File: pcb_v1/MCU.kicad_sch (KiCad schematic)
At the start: 12 parts, among them U4 ESP32-S3-MINI-1, U6 STM32F103RETx

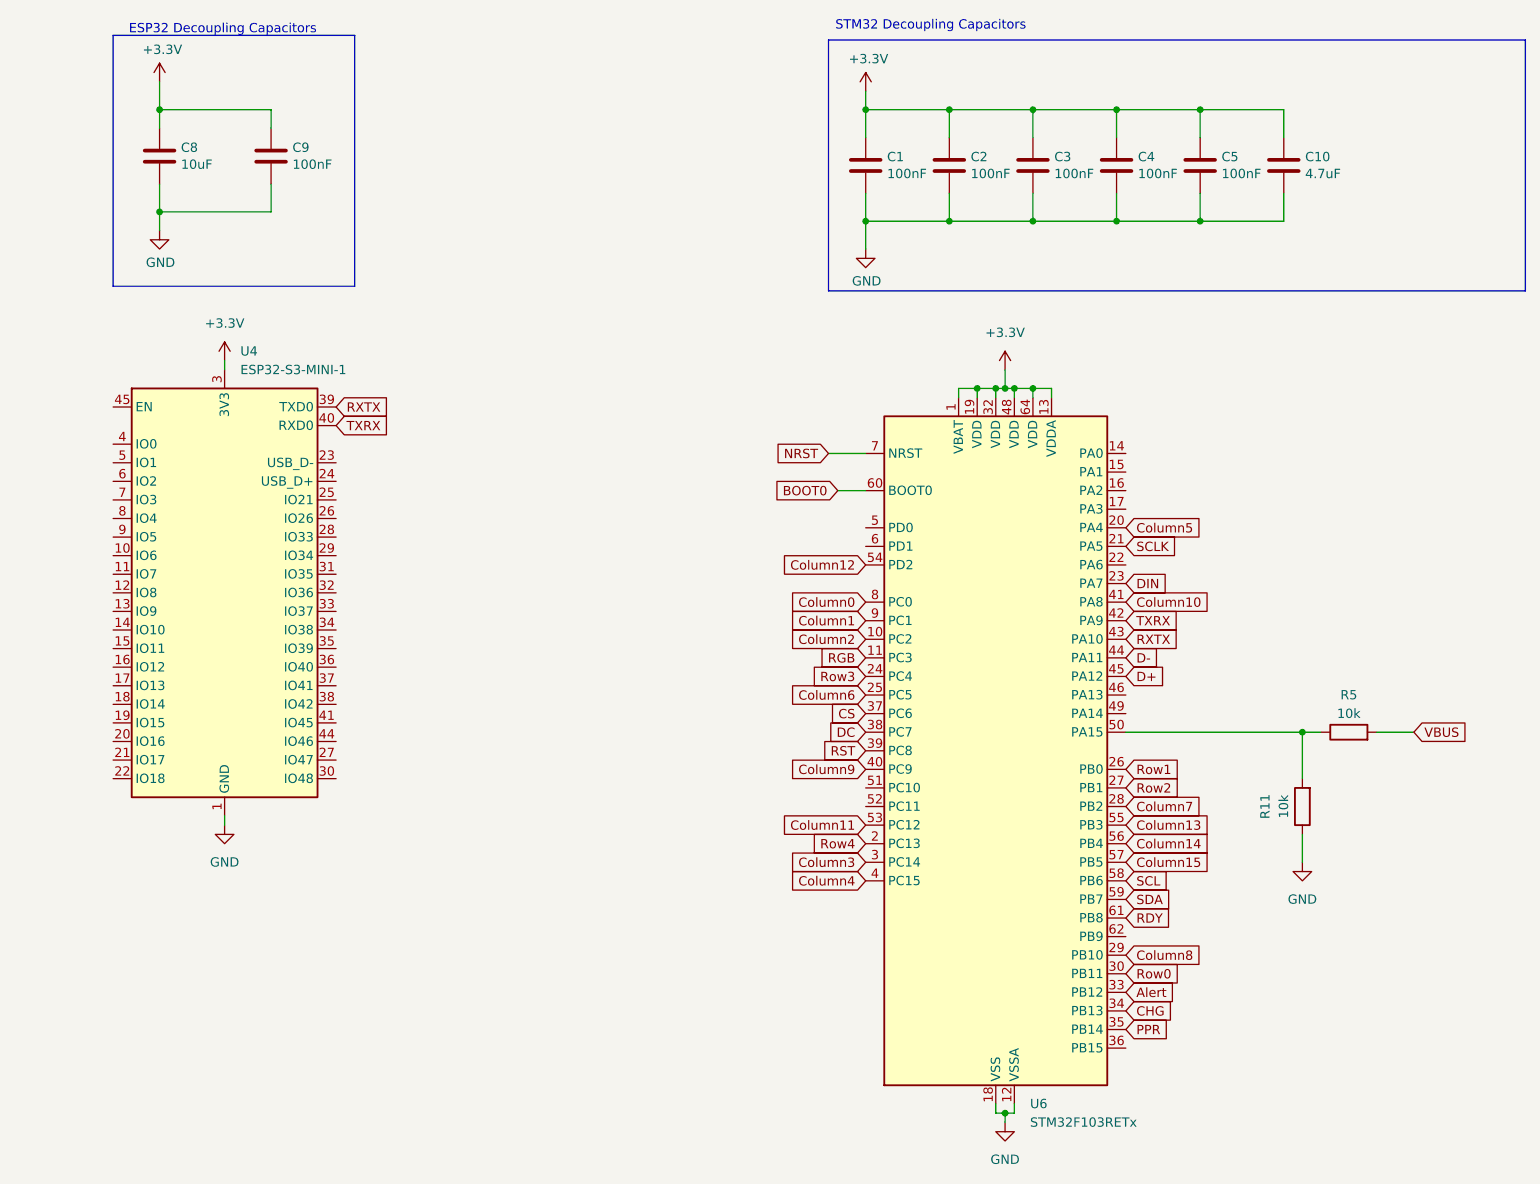
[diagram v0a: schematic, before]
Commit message: Finished 4 layer design
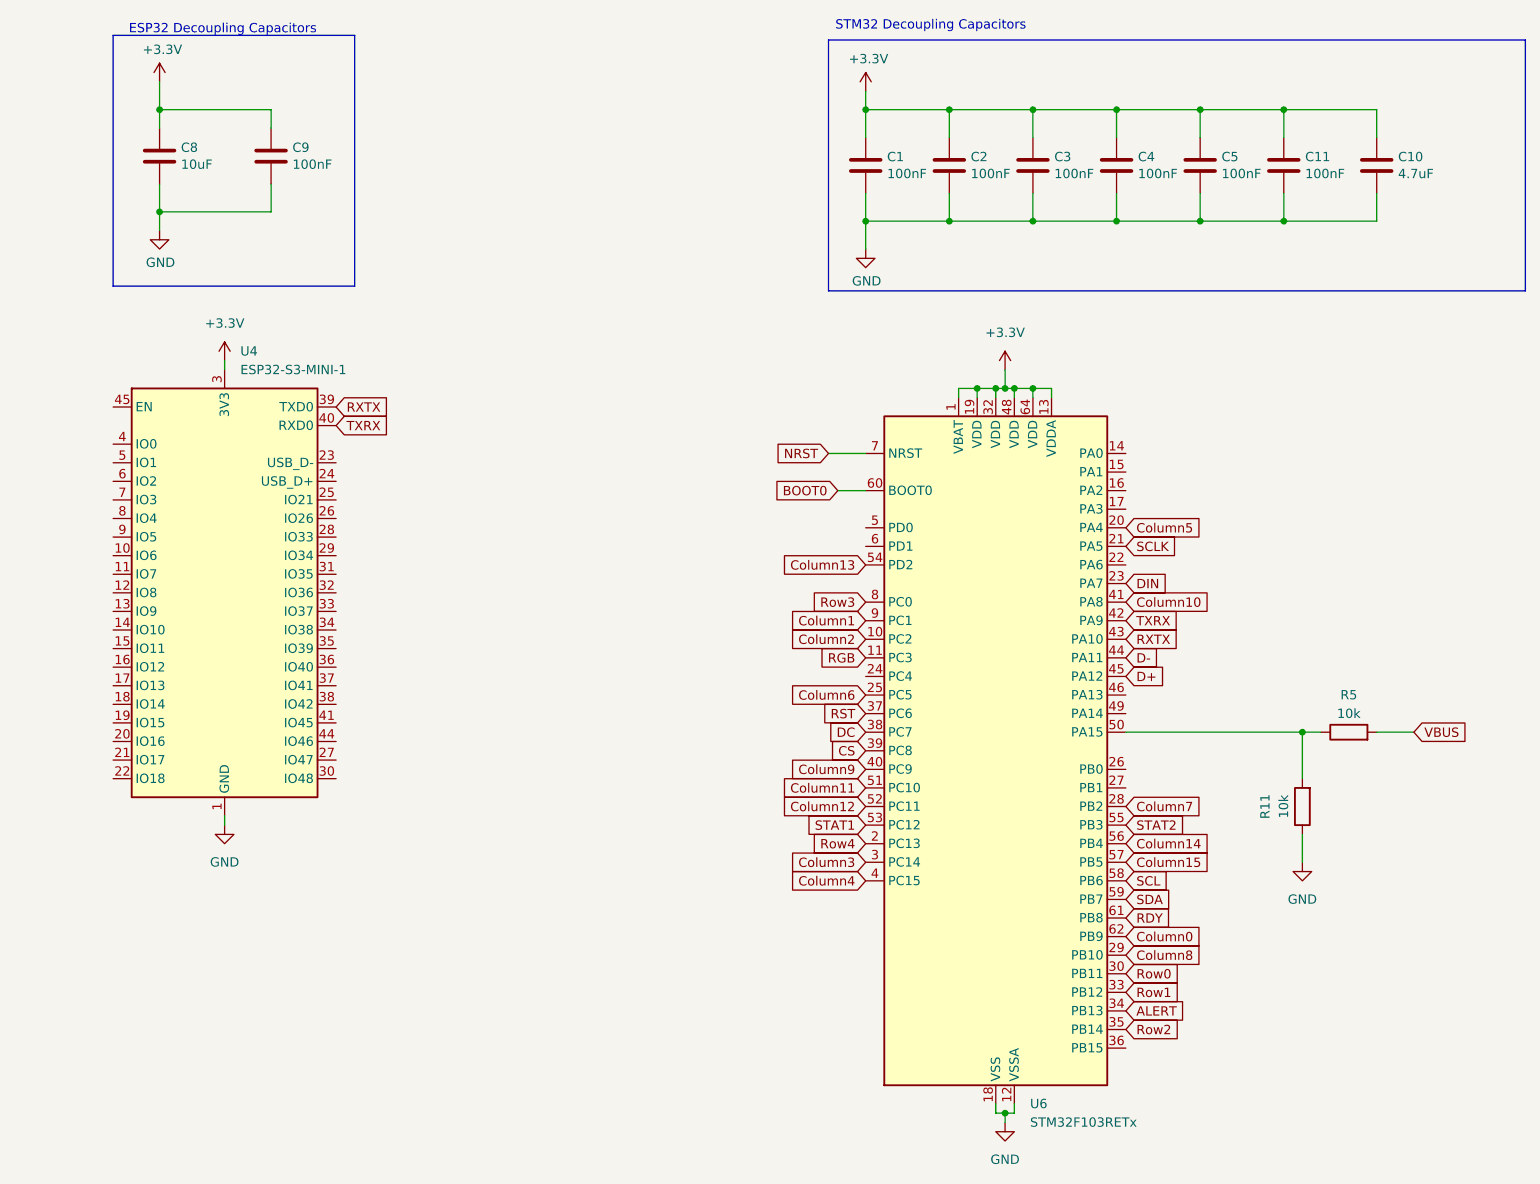
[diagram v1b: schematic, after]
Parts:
- added C11: 100nF, GRM1555C2A101GA01D:CAPC1005X55N, symbol Device:C
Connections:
- net Alert is gone; now on net Row1: U6.33 (PB12)
- net PPR is gone; now on net Row2: U6.35 (PB14)
- net +3.3V: now also C11.1
- net CS: now also U6.39 (PC8); no longer U6.37 (PC6)
- net Column0: now also U6.62 (PB9); no longer U6.8 (PC0)
- net Column11: now also U6.51 (PC10); no longer U6.53 (PC12)
- net Column12: now also U6.52 (PC11); no longer U6.54 (PD2)
- net Column13: now also U6.54 (PD2); no longer U6.55 (PB3)
- net GND: now also C11.2
- net RST: now also U6.37 (PC6); no longer U6.39 (PC8)
- net Row1: no longer U6.26 (PB0)
- net Row2: no longer U6.27 (PB1)
- net Row3: now also U6.8 (PC0); no longer U6.24 (PC4)
- net CHG renamed ALERT
- new net STAT1: U6.53 (PC12)
- new net STAT2: U6.55 (PB3)
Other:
- moved on the sheet: C10

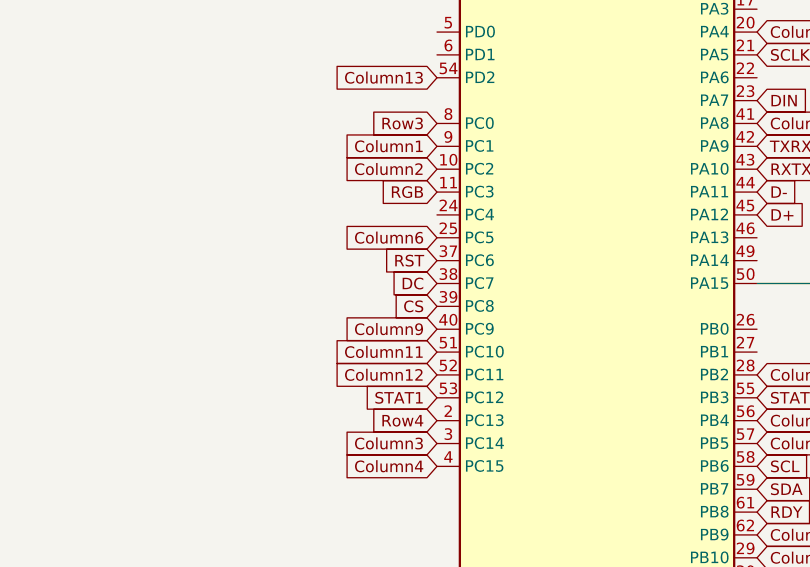
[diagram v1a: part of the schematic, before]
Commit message: Reverse polarity on pins
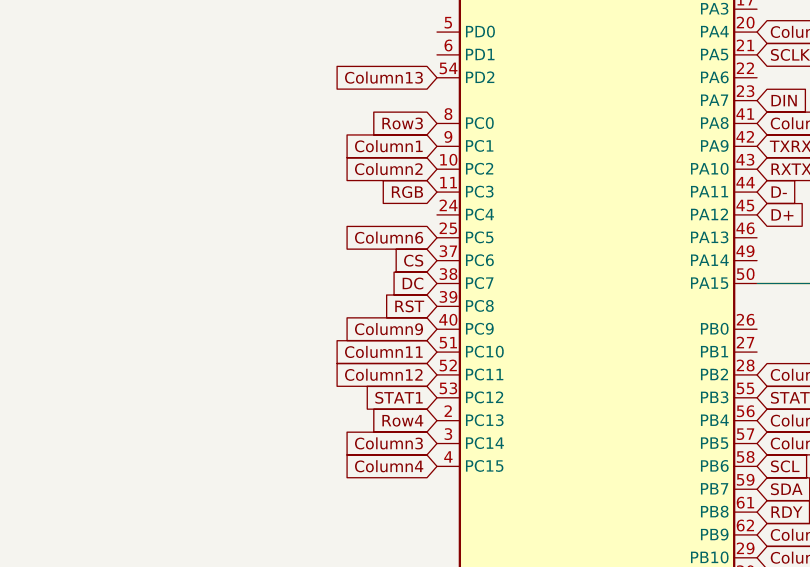
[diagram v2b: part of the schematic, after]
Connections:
- net CS: now also U6.37 (PC6); no longer U6.39 (PC8)
- net RST: now also U6.39 (PC8); no longer U6.37 (PC6)
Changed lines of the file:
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@@
+		)
+	)
+	(global_label "RST"
+		(shape input)
+		(at 127 118.11 180)
+		(fields_autoplaced yes)
+		(effects
+			(font
+				(size 1.27 1.27)
+			)
+			(justify right)
+		)
+		(property "Intersheetrefs" "${INTERSHEET_REFS}"
+			(at 120.5677 118.11 0)
+			(effects
+				(font
+					(size 1.27 1.27)
+				)
+				(justify right)
+				(hide yes)
+			)
 		)
 	)
@@
 		)
 	)
+	(global_label "CS"
+		(shape input)
+		(at 127 113.03 180)
+		(fields_autoplaced yes)
+		(effects
+			(font
+				(size 1.27 1.27)
+			)
+			(justify right)
+		)
+		(property "Intersheetrefs" "${INTERSHEET_REFS}"
+			(at 121.5353 113.03 0)
+			(effects
+				(font
+					(size 1.27 1.27)
+				)
+				(justify right)
+				(hide yes)
+			)
+		)
+	)
 	(global_label "RXTX"
 		(shape input)
@@
 		)
 	)
-	(global_label "CS"
-		(shape input)
-		(at 127 118.11 180)
-		(fields_autoplaced yes)
-		(effects
-			(font
-				(size 1.27 1.27)
-			)
-			(justify right)
-		)
-		(property "Intersheetrefs" "${INTERSHEET_REFS}"
-			(at 121.5353 118.11 0)
-			(effects
-				(font
-					(size 1.27 1.27)
-				)
-				(justify right)
-				(hide yes)
-			)
-		)
-	)
 	(global_label "Column12"
 		(shape input)
@@
 				(hide yes)
 			)
-		)
-	)
-	(global_label "RST"
-		(shape input)
-		(at 127 113.03 180)
-		(fields_autoplaced yes)
-		(effects
-			(font
-				(size 1.27 1.27)
-			)
-			(justify right)
-		)
-		(property "Intersheetrefs" "${INTERSHEET_REFS}"
-			(at 120.5677 113.03 0)
-			(effects
-				(font
-					(size 1.27 1.27)
-				)
-				(justify right)
-				(hide yes)
-			)

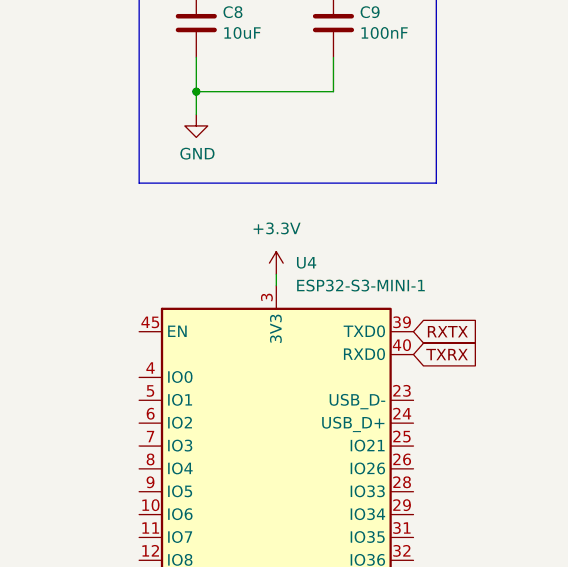
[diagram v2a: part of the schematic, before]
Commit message: Included resistors for EN/GPIO0 on ESP32
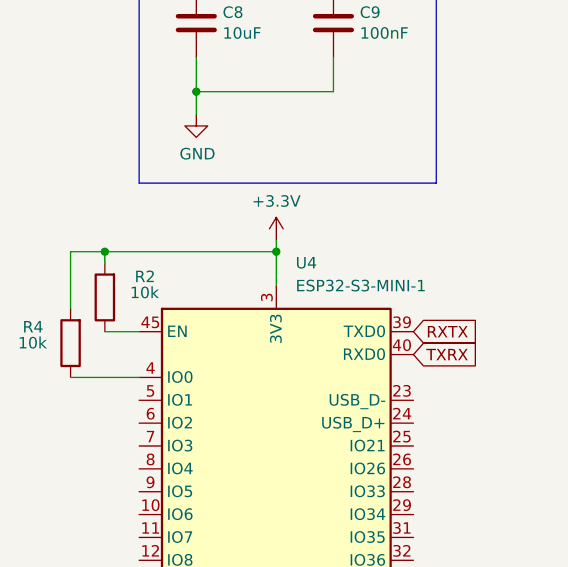
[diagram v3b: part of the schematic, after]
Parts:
- added R2, R4: 10k, RC0402FR-7D4K7L:RESC1005X40N, symbol ScottoKeebs:Placeholder_Resistor
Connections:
- net +3.3V: now also R2.2, R4.2
- net at U4.4 (IO0): now also R4.1
- net at U4.45 (EN): now also R2.1
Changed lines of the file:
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@@
 	)
 	(junction
+		(at 20.32 62.23)
+		(diameter 0)
+		(color 0 0 0 0)
+	)
+	(junction
 		(at 127 45.72)
 		(diameter 0)
@@
 		(color 0 0 0 0)
 	)
+	(junction
+		(at 39.37 62.23)
+		(diameter 0)
+		(color 0 0 0 0)
+	)
 	(wire
 		(pts
@@
 	(wire
 		(pts
+			(xy 16.51 68.58) (xy 16.51 62.23)
+		)
+		(stroke
+			(width 0)
+			(type default)
+		)
+	)
+	(wire
+		(pts
 			(xy 186.69 115.57) (xy 189.23 115.57)
 		)
@@
 	(wire
 		(pts
+			(xy 16.51 76.2) (xy 24.13 76.2)
+		)
+		(stroke
+			(width 0)
+			(type default)
+		)
+	)
+	(wire
+		(pts
 			(xy 127 45.72) (xy 127 49.53)
 		)
@@
 	(wire
 		(pts
+			(xy 20.32 62.23) (xy 20.32 63.5)
+		)
+		(stroke
+			(width 0)
+			(type default)
+		)
+	)
+	(wire
+		(pts
 			(xy 30.48 33.02) (xy 30.48 30.48)
 		)
@@
 	(wire
 		(pts
+			(xy 39.37 60.96) (xy 39.37 62.23)
+		)
+		(stroke
+			(width 0)
+			(type default)
+		)
+	)
+	(wire
+		(pts
 			(xy 45.72 44.45) (xy 45.72 40.64)
 		)
@@
 	(wire
 		(pts
+			(xy 20.32 71.12) (xy 24.13 71.12)
+		)
+		(stroke
+			(width 0)
+			(type default)
+		)
+	)
+	(wire
+		(pts
 			(xy 144.78 167.64) (xy 146.05 167.64)
 		)
@@
 	(wire
 		(pts
-			(xy 39.37 64.77) (xy 39.37 66.04)
+			(xy 20.32 62.23) (xy 39.37 62.23)
+		)
+		(stroke
+			(width 0)
+			(type default)
+		)
+	)
+	(wire
+		(pts
+			(xy 39.37 62.23) (xy 39.37 66.04)
 		)
 		(stroke
@@
 	(wire
 		(pts
+			(xy 16.51 62.23) (xy 20.32 62.23)
+		)
+		(stroke
+			(width 0)
+			(type default)
+		)
+	)
+	(wire
+		(pts
 			(xy 161.29 30.48) (xy 161.29 34.29)
 		)
@@
 	(symbol
 		(lib_id "power:+3.3V")
-		(at 39.37 64.77 0)
+		(at 39.37 60.96 0)
 		(unit 1)
 		(exclude_from_sim no)
@@
 		(on_board yes)
 		(dnp no)
-		(fields_autoplaced yes)
 		(property "Reference" "#PWR024"
-			(at 39.37 68.58 0)
+			(at 39.37 64.77 0)
 			(effects
 				(font
@@
 		)
 		(property "Value" "+3.3V"
-			(at 39.37 59.69 0)
+			(at 39.37 56.642 0)
 			(effects
 				(font
@@
 		)
 		(property "Footprint" ""
-			(at 39.37 64.77 0)
+			(at 39.37 60.96 0)
 			(effects
 				(font
@@
 		)
 		(property "Datasheet" ""
-			(at 39.37 64.77 0)
+			(at 39.37 60.96 0)
 			(effects
 				(font
@@
 		)
 		(property "Description" "Power symbol creates a global label with name \"+3.3V\""
-			(at 39.37 64.77 0)
+			(at 39.37 60.96 0)
 			(effects
 				(font
@@
 	)
 	(symbol
+		(lib_id "ScottoKeebs:Placeholder_Resistor")
+		(at 16.51 72.39 90)
+		(unit 1)
+		(exclude_from_sim no)
+		(in_bom yes)
+		(on_board yes)
+		(dnp no)
+		(property "Reference" "R4"
+			(at 11.176 70.612 90)
+			(effects
+				(font
+					(size 1.27 1.27)
+				)
+				(justify right)
+			)
+		)
+		(property "Value" "10k"
+			(at 10.668 72.39 90)
+			(effects
+				(font
+					(size 1.27 1.27)
+				)
+				(justify right)
+			)
+		)
+		(property "Footprint" "RC0402FR-7D4K7L:RESC1005X40N"
+			(at 18.288 72.39 0)
+			(effects
+				(font
+					(size 1.27 1.27)
+				)
+				(hide yes)
+			)
+		)
+		(property "Datasheet" "~"
+			(at 16.51 72.39 90)
+			(effects
+				(font
+					(size 1.27 1.27)
+				)
+				(hide yes)
+			)
+		)
+		(property "Description" "Resistor"
+			(at 16.51 72.39 0)
+			(effects
+				(font
+					(size 1.27 1.27)
+				)
+				(hide yes)
+			)
+		)
+		(pin "2"
+		)
+		(pin "1"
+		)
+		(instances
+			(project "pcb_v1"
+				(path "/bf36a815-88b9-4f95-84c3-6b01513341e6/72f05775-4420-4660-b628-1f03fc3d3776"
+					(reference "R4")
+					(unit 1)
+				)
+			)
+		)
+	)
+	(symbol
 		(lib_id "Device:C")
 		(at 161.29 38.1 0)
@@
 					(unit 1)
 				)
+			)
+		)
+	)
+	(symbol
+		(lib_id "ScottoKeebs:Placeholder_Resistor")
+		(at 20.32 67.31 90)
+		(unit 1)
+		(exclude_from_sim no)
+		(in_bom yes)
+		(on_board yes)
+		(dnp no)
+		(property "Reference" "R2"
+			(at 23.622 65.024 90)
+			(effects
+				(font
+					(size 1.27 1.27)
+				)
+				(justify right)
+			)
+		)
+		(property "Value" "10k"
+			(at 23.114 66.802 90)
+			(effects
+				(font
+					(size 1.27 1.27)
+				)
+				(justify right)
+			)
+		)
+		(property "Footprint" "RC0402FR-7D4K7L:RESC1005X40N"
+			(at 22.098 67.31 0)
+			(effects
+				(font
+					(size 1.27 1.27)
+				)
+				(hide yes)
+			)
+		)
+		(property "Datasheet" "~"
+			(at 20.32 67.31 90)
+			(effects
+				(font
+					(size 1.27 1.27)
+				)
+				(hide yes)
+			)
+		)
+		(property "Description" "Resistor"
+			(at 20.32 67.31 0)
+			(effects
+				(font
+					(size 1.27 1.27)
+				)
+				(hide yes)
+			)
+		)
+		(pin "2"
+		)
+		(pin "1"
+		)
+		(instances
+			(project ""
+				(path "/bf36a815-88b9-4f95-84c3-6b01513341e6/72f05775-4420-4660-b628-1f03fc3d3776"
+					(reference "R2")
+					(unit 1)
+				)
